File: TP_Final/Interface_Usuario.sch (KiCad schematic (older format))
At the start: 31 parts, among them J108 BG2, Q105 2N3904, Q106 2N3904, Q107 2N3904, SW102 KSR, SW103 KSR, SW104 KSR, SW105 KSR

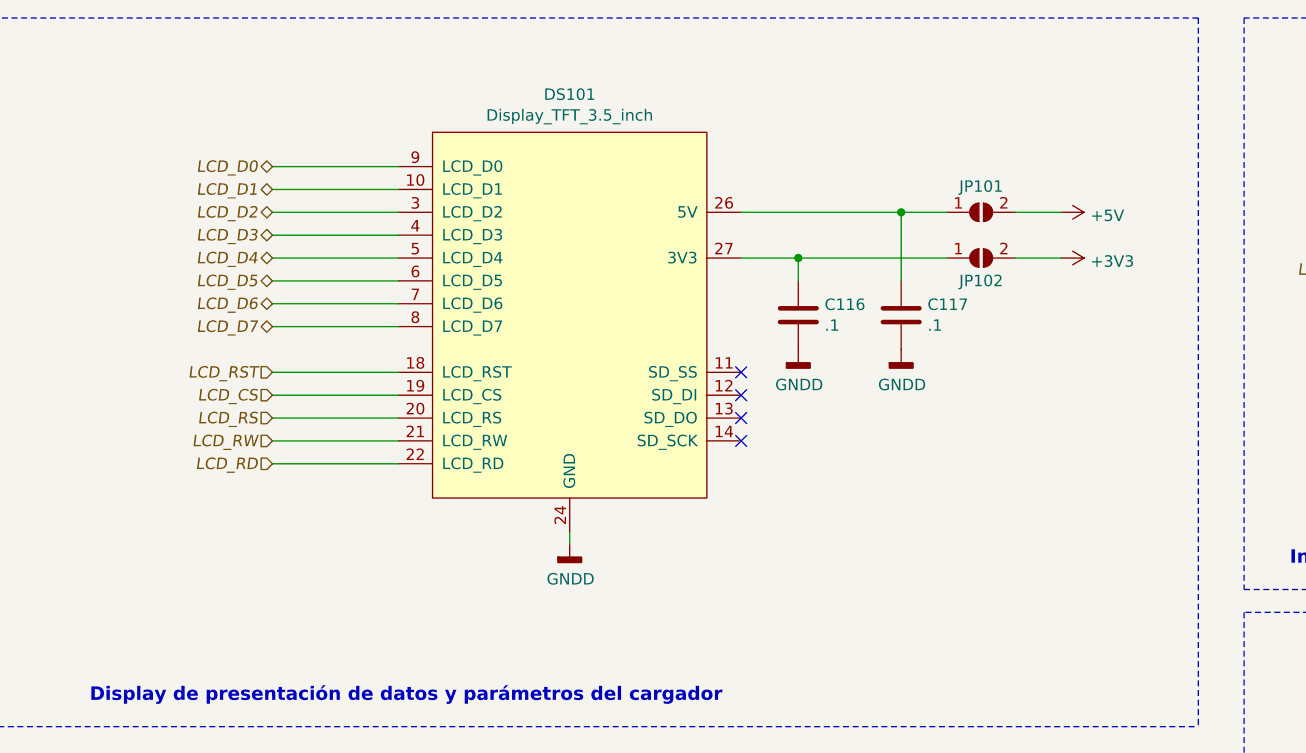
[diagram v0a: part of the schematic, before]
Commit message: Se completa rotulo
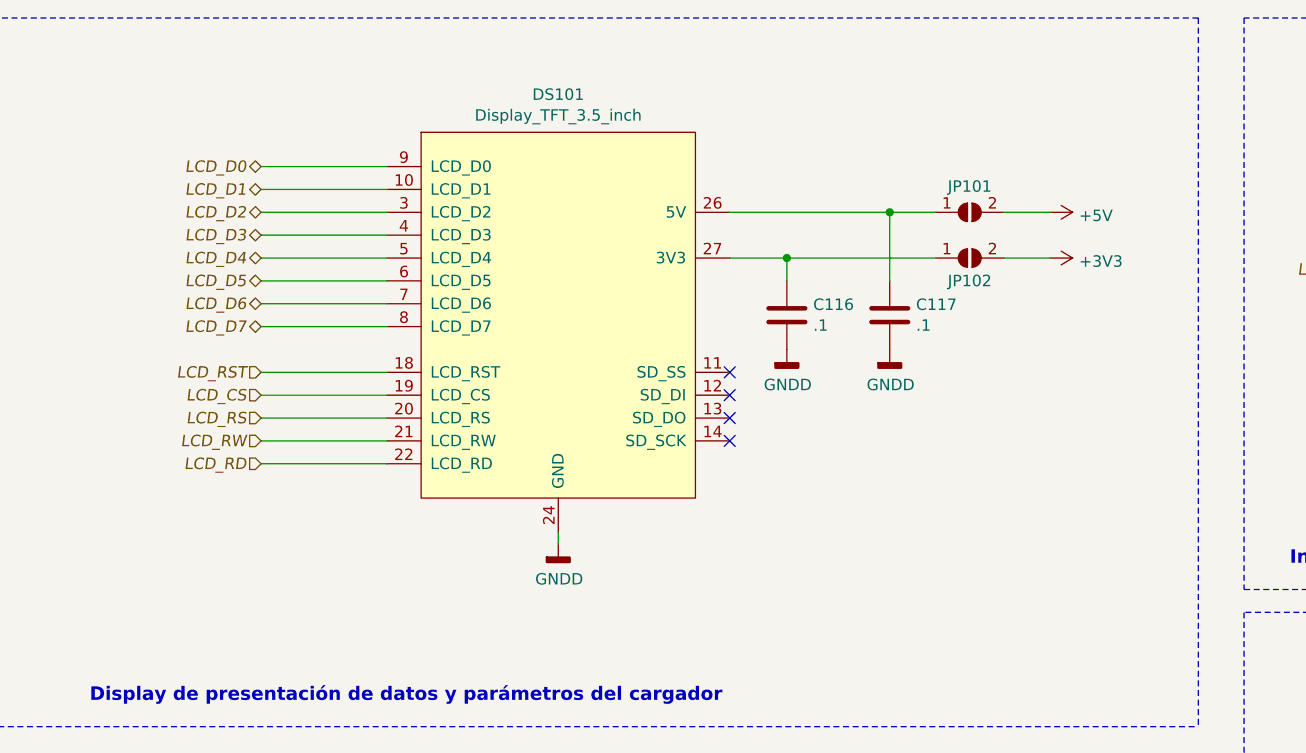
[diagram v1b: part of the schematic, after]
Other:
- moved on the sheet: C116, C117, DS101, JP101, JP102
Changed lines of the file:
@@
 Sheet 3 4
 Title "Cargador modular de baterias industriales"
-Date "2021-03-18"
-Rev "0"
+Date "2021-03-26"
+Rev "1"
 Comp "proba"
-Comment1 "Revisor: Diego Brengi"
-Comment2 "Autor: Felipe A. Calcavecchia"
-Comment3 ""
-Comment4 ""
+Comment1 "Creative Commons Attribution-NonCommercial-ShareAlike 4.0 International License"
+Comment2 "Revisor 2: Cristian A. Trinidad"
+Comment3 "Revisor 1: Diego Brengi"
+Comment4 "Autor: Felipe A. Calcavecchia"
 $EndDescr
 $Comp
@@
 	8950 3850 8950 3750
 Wire Wire Line
-	3150 1200 3700 1200
-Wire Wire Line
-	3150 1300 3700 1300
-Wire Wire Line
-	3150 1400 3700 1400
-Wire Wire Line
-	3150 1500 3700 1500
-Wire Wire Line
-	3150 1600 3700 1600
-Wire Wire Line
-	3150 1700 3700 1700
-Wire Wire Line
-	3150 1800 3700 1800
-Wire Wire Line
-	3150 1900 3700 1900
+	3100 1200 3650 1200
+Wire Wire Line
+	3100 1300 3650 1300
+Wire Wire Line
+	3100 1400 3650 1400
+Wire Wire Line
+	3100 1500 3650 1500
+Wire Wire Line
+	3100 1600 3650 1600
+Wire Wire Line
+	3100 1700 3650 1700
+Wire Wire Line
+	3100 1800 3650 1800
+Wire Wire Line
+	3100 1900 3650 1900
 Wire Wire Line
 	8100 1650 8350 1650
@@
 	8100 2250 8350 2250
 Wire Wire Line
-	3700 2100 3150 2100
-Wire Wire Line
-	3700 2200 3150 2200
-Wire Wire Line
-	3700 2300 3150 2300
-Wire Wire Line
-	3700 2400 3150 2400
-Wire Wire Line
-	3700 2500 3150 2500
-Text HLabel 3150 1400 0    50   BiDi Italic 0
+	3650 2100 3100 2100
+Wire Wire Line
+	3650 2200 3100 2200
+Wire Wire Line
+	3650 2300 3100 2300
+Wire Wire Line
+	3650 2400 3100 2400
+Wire Wire Line
+	3650 2500 3100 2500
+Text HLabel 3100 1400 0    50   BiDi Italic 0
 LCD_D2
-Text HLabel 3150 1500 0    50   BiDi Italic 0
+Text HLabel 3100 1500 0    50   BiDi Italic 0
 LCD_D3
-Text HLabel 3150 1600 0    50   BiDi Italic 0
+Text HLabel 3100 1600 0    50   BiDi Italic 0
 LCD_D4
-Text HLabel 3150 1700 0    50   BiDi Italic 0
+Text HLabel 3100 1700 0    50   BiDi Italic 0
 LCD_D5
-Text HLabel 3150 1800 0    50   BiDi Italic 0
+Text HLabel 3100 1800 0    50   BiDi Italic 0
 LCD_D6
-Text HLabel 3150 1900 0    50   BiDi Italic 0
+Text HLabel 3100 1900 0    50   BiDi Italic 0
 LCD_D7
-Text HLabel 3150 1200 0    50   BiDi Italic 0
+Text HLabel 3100 1200 0    50   BiDi Italic 0
 LCD_D0
-Text HLabel 3150 1300 0    50   BiDi Italic 0
+Text HLabel 3100 1300 0    50   BiDi Italic 0
 LCD_D1
-Text HLabel 3150 2100 0    50   Input Italic 0
+Text HLabel 3100 2100 0    50   Input Italic 0
 LCD_RST
-Text HLabel 3150 2200 0    50   Input Italic 0
+Text HLabel 3100 2200 0    50   Input Italic 0
 LCD_CS
-Text HLabel 3150 2300 0    50   Input Italic 0
+Text HLabel 3100 2300 0    50   Input Italic 0
 LCD_RS
-Text HLabel 3150 2400 0    50   Input Italic 0
+Text HLabel 3100 2400 0    50   Input Italic 0
 LCD_RW
-Text HLabel 3150 2500 0    50   Input Italic 0
+Text HLabel 3100 2500 0    50   Input Italic 0
 LCD_RD
 Text HLabel 8100 1650 0    50   Input Italic 0
@@
 L Jumper:SolderJumper_2_Open JP101
 U 1 1 609BD0C4
-P 6250 1400
-F 0 "JP101" H 6250 1513 50  0000 C CNN
-F 1 "SolderJumper_2_Open" H 6250 1514 50  0001 C CNN
-F 2 "Jumper:SolderJumper-2_P1.3mm_Open_RoundedPad1.0x1.5mm" H 6250 1400 50  0001 C CNN
-F 3 "~" H 6250 1400 50  0001 C CNN
-	1    6250 1400
+P 6200 1400
+F 0 "JP101" H 6200 1513 50  0000 C CNN
+F 1 "SolderJumper_2_Open" H 6200 1514 50  0001 C CNN
+F 2 "Jumper:SolderJumper-2_P1.3mm_Open_RoundedPad1.0x1.5mm" H 6200 1400 50  0001 C CNN
+F 3 "~" H 6200 1400 50  0001 C CNN
+	1    6200 1400
 	1    0    0    -1
 $EndComp
@@
 L Jumper:SolderJumper_2_Open JP102
 U 1 1 609BE636
-P 6250 1600
-F 0 "JP102" H 6250 1500 50  0000 C CNN
-F 1 "SolderJumper_2_Open" H 6250 1714 50  0001 C CNN
-F 2 "Jumper:SolderJumper-2_P1.3mm_Open_RoundedPad1.0x1.5mm" H 6250 1600 50  0001 C CNN
-F 3 "~" H 6250 1600 50  0001 C CNN
-	1    6250 1600
+P 6200 1600
+F 0 "JP102" H 6200 1500 50  0000 C CNN
+F 1 "SolderJumper_2_Open" H 6200 1714 50  0001 C CNN
+F 2 "Jumper:SolderJumper-2_P1.3mm_Open_RoundedPad1.0x1.5mm" H 6200 1600 50  0001 C CNN
+F 3 "~" H 6200 1600 50  0001 C CNN
+	1    6200 1600
 	1    0    0    -1
 $EndComp
@@
 L power:+3V3 #PWR0150
 U 1 1 609BEA8F
-P 6600 1600
-F 0 "#PWR0150" H 6600 1450 50  0001 C CNN
-F 1 "+3V3" V 6615 1728 50  0000 L CNN
-F 2 "" H 6600 1600 50  0001 C CNN
-F 3 "" H 6600 1600 50  0001 C CNN
-	1    6600 1600
+P 6550 1600
+F 0 "#PWR0150" H 6550 1450 50  0001 C CNN
+F 1 "+3V3" V 6565 1728 50  0000 L CNN
+F 2 "" H 6550 1600 50  0001 C CNN
+F 3 "" H 6550 1600 50  0001 C CNN
+	1    6550 1600
 	0    1    1    0
 $EndComp
@@
 L power:+5V #PWR0148
 U 1 1 609BF4A5
-P 6600 1400
-F 0 "#PWR0148" H 6600 1250 50  0001 C CNN
-F 1 "+5V" V 6615 1528 50  0000 L CNN
-F 2 "" H 6600 1400 50  0001 C CNN
-F 3 "" H 6600 1400 50  0001 C CNN
-	1    6600 1400
+P 6550 1400
+F 0 "#PWR0148" H 6550 1250 50  0001 C CNN
+F 1 "+5V" V 6565 1528 50  0000 L CNN
+F 2 "" H 6550 1400 50  0001 C CNN
+F 3 "" H 6550 1400 50  0001 C CNN
+	1    6550 1400
 	0    1    1    0
 $EndComp
@@
 L Device:C C117
 U 1 1 609BFCB6
-P 5900 1850
-F 0 "C117" H 6015 1896 50  0000 L CNN
-F 1 ".1" H 6015 1805 50  0000 L CNN
-F 2 "Capacitor_SMD:C_0805_2012Metric" H 5938 1700 50  0001 C CNN
-F 3 "~" H 5900 1850 50  0001 C CNN
-	1    5900 1850
+P 5850 1850
+F 0 "C117" H 5965 1896 50  0000 L CNN
+F 1 ".1" H 5965 1805 50  0000 L CNN
+F 2 "Capacitor_SMD:C_0805_2012Metric" H 5888 1700 50  0001 C CNN
+F 3 "~" H 5850 1850 50  0001 C CNN
+	1    5850 1850
 	1    0    0    -1
 $EndComp
@@
 L Device:C C116
 U 1 1 609C084D
-P 5450 1850
-F 0 "C116" H 5565 1896 50  0000 L CNN
-F 1 ".1" H 5565 1805 50  0000 L CNN
-F 2 "Capacitor_SMD:C_0805_2012Metric" H 5488 1700 50  0001 C CNN
-F 3 "~" H 5450 1850 50  0001 C CNN
-	1    5450 1850
+P 5400 1850
+F 0 "C116" H 5515 1896 50  0000 L CNN
+F 1 ".1" H 5515 1805 50  0000 L CNN
+F 2 "Capacitor_SMD:C_0805_2012Metric" H 5438 1700 50  0001 C CNN
+F 3 "~" H 5400 1850 50  0001 C CNN
+	1    5400 1850
 	1    0    0    -1
 $EndComp
@@
 L power:GNDD #PWR0152
 U 1 1 609C159B
-P 5450 2000
-F 0 "#PWR0152" H 5450 1750 50  0001 C CNN
-F 1 "GNDD" H 5454 1845 50  0000 C CNN
-F 2 "" H 5450 2000 50  0001 C CNN
-F 3 "" H 5450 2000 50  0001 C CNN
-	1    5450 2000
+P 5400 2000
+F 0 "#PWR0152" H 5400 1750 50  0001 C CNN
+F 1 "GNDD" H 5404 1845 50  0000 C CNN
+F 2 "" H 5400 2000 50  0001 C CNN
+F 3 "" H 5400 2000 50  0001 C CNN
+	1    5400 2000
 	1    0    0    -1
 $EndComp
@@
 L power:GNDD #PWR0153
 U 1 1 609C1EED
-P 5900 2000
-F 0 "#PWR0153" H 5900 1750 50  0001 C CNN
-F 1 "GNDD" H 5904 1845 50  0000 C CNN
-F 2 "" H 5900 2000 50  0001 C CNN
-F 3 "" H 5900 2000 50  0001 C CNN
-	1    5900 2000
-	1    0    0    -1
-$EndComp
-Wire Wire Line
-	5200 1600 5450 1600
-Wire Wire Line
-	6400 1600 6600 1600
-Wire Wire Line
-	6600 1400 6400 1400
-Wire Wire Line
-	5900 1700 5900 1400
-Wire Wire Line
-	5900 1400 6100 1400
-Wire Wire Line
-	5450 1700 5450 1600
-Connection ~ 5450 1600
-Wire Wire Line
-	5450 1600 6100 1600
+P 5850 2000
+F 0 "#PWR0153" H 5850 1750 50  0001 C CNN
+F 1 "GNDD" H 5854 1845 50  0000 C CNN
+F 2 "" H 5850 2000 50  0001 C CNN
+F 3 "" H 5850 2000 50  0001 C CNN
+	1    5850 2000
+	1    0    0    -1
+$EndComp
+Wire Wire Line
+	5150 1600 5400 1600
+Wire Wire Line
+	6350 1600 6550 1600
+Wire Wire Line
+	6550 1400 6350 1400
+Wire Wire Line
+	5850 1700 5850 1400
+Wire Wire Line
+	5850 1400 6050 1400
+Wire Wire Line
+	5400 1700 5400 1600
+Connection ~ 5400 1600
+Wire Wire Line
+	5400 1600 6050 1600
 Text HLabel 8000 5450 0    50   Output Italic 0
 P.E.
@@
 	8400 5450 8000 5450
 Wire Wire Line
-	5200 1400 5900 1400
-Connection ~ 5900 1400
+	5150 1400 5850 1400
+Connection ~ 5850 1400
 Wire Notes Line
 	7200 550  1950 550
@@
 L New_Library:Display_TFT_3.5_inch DS101
 U 1 1 6058B937
-P 4450 1800
-F 0 "DS101" H 4450 2715 50  0000 C CNN
-F 1 "Display_TFT_3.5_inch" H 4450 2624 50  0000 C CNN
-F 2 "TP_Final:Display_TFT_3.5_inch" H 3850 2200 50  0001 C CNN
-F 3 "" H 3850 2200 50  0001 C CNN
-	1    4450 1800
-	1    0    0    -1
-$EndComp
-NoConn ~ 5200 2100
-NoConn ~ 5200 2200
-NoConn ~ 5200 2300
-NoConn ~ 5200 2400
+P 4400 1800
+F 0 "DS101" H 4400 2715 50  0000 C CNN
+F 1 "Display_TFT_3.5_inch" H 4400 2624 50  0000 C CNN
+F 2 "TP_Final:Display_TFT_3.5_inch" H 3800 2200 50  0001 C CNN
+F 3 "" H 3800 2200 50  0001 C CNN
+	1    4400 1800
+	1    0    0    -1
+$EndComp
+NoConn ~ 5150 2100
+NoConn ~ 5150 2200
+NoConn ~ 5150 2300
+NoConn ~ 5150 2400
 $Comp
 L power:GNDD #PWR0155
 U 1 1 605D4150
-P 4450 2850
-F 0 "#PWR0155" H 4450 2600 50  0001 C CNN
-F 1 "GNDD" H 4454 2695 50  0000 C CNN
-F 2 "" H 4450 2850 50  0001 C CNN
-F 3 "" H 4450 2850 50  0001 C CNN
-	1    4450 2850
-	1    0    0    -1
-$EndComp
-Wire Wire Line
-	4450 2850 4450 2800
+P 4400 2850
+F 0 "#PWR0155" H 4400 2600 50  0001 C CNN
+F 1 "GNDD" H 4404 2695 50  0000 C CNN
+F 2 "" H 4400 2850 50  0001 C CNN
+F 3 "" H 4400 2850 50  0001 C CNN
+	1    4400 2850
+	1    0    0    -1
+$EndComp
+Wire Wire Line
+	4400 2850 4400 2800
 $EndSCHEMATC
